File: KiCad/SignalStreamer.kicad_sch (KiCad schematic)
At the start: 24 parts, among them J101 Conn_01x01, J102 Conn_01x01, J103 Conn_01x01, J104 Conn_01x01, J105 Conn_01x02, T101 Coupled_Inductors_2

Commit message: Ver X1.0
Copied latest changes from backup project
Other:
- sheet Hardware: file untitled.kicad_sch -> hardware.kicad_sch
- title: 80m Vertical Dipole Fox Antenna -> 80m Bottom-Loaded Vertical Fox Antenna
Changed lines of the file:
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@@
 	(generator "eeschema")
 	(generator_version "9.0")
-	(paper "A4")
+	(paper "USLetter")
 	(title_block
-		(title "80m Vertical Dipole Fox Antenna")
-		(date "2025-12-30")
+		(title "80m Bottom-Loaded Vertical Fox Antenna")
+		(date "2026-01-02")
 		(rev "X1.0")
 	)
@@
 			)
 		)
+		(property "Sim.Enable" ""
+			(at 191.77 97.79 0)
+			(effects
+				(font
+					(size 1.27 1.27)
+				)
+				(hide yes)
+			)
+		)
 		(pin "1"
 		)
@@
 			)
 		)
+		(property "Sim.Enable" ""
+			(at 123.19 93.98 0)
+			(effects
+				(font
+					(size 1.27 1.27)
+				)
+				(hide yes)
+			)
+		)
 		(pin "4"
 		)
@@
 			)
 		)
+		(property "Sim.Enable" ""
+			(at 113.03 114.3 0)
+			(effects
+				(font
+					(size 1.27 1.27)
+				)
+				(hide yes)
+			)
+		)
 		(pin "1"
 		)
@@
 			)
 		)
-		(property "Sim.Device" ""
-			(at 218.44 97.79 0)
-			(effects
-				(font
-					(size 1.27 1.27)
-				)
-				(hide yes)
-			)
-		)
-		(property "Sim.Pins" ""
-			(at 218.44 97.79 0)
-			(effects
-				(font
-					(size 1.27 1.27)
-				)
-				(hide yes)
-			)
-		)
 		(property "Sim.Enable" ""
 			(at 218.44 97.79 0)
@@
 			)
 		)
+		(property "Sim.Enable" ""
+			(at 140.97 93.98 90)
+			(effects
+				(font
+					(size 1.27 1.27)
+				)
+				(hide yes)
+			)
+		)
 		(pin "1"
 		)
@@
 			)
 		)
-		(property "Sim.Device" ""
-			(at 241.3 97.79 0)
-			(effects
-				(font
-					(size 1.27 1.27)
-				)
-				(hide yes)
-			)
-		)
-		(property "Sim.Pins" ""
-			(at 241.3 97.79 0)
-			(effects
-				(font
-					(size 1.27 1.27)
-				)
-				(hide yes)
-			)
-		)
 		(property "Sim.Enable" ""
 			(at 241.3 97.79 0)
@@
 			)
 		)
-		(property "Sim.Device" ""
-			(at 229.87 97.79 0)
-			(effects
-				(font
-					(size 1.27 1.27)
-				)
-				(hide yes)
-			)
-		)
-		(property "Sim.Pins" ""
-			(at 229.87 97.79 0)
-			(effects
-				(font
-					(size 1.27 1.27)
-				)
-				(hide yes)
-			)
-		)
 		(property "Sim.Enable" ""
 			(at 229.87 97.79 0)
@@
 			)
 		)
-		(property "Sim.Device" ""
-			(at 205.74 97.79 0)
-			(effects
-				(font
-					(size 1.27 1.27)
-				)
-				(hide yes)
-			)
-		)
-		(property "Sim.Pins" ""
-			(at 205.74 97.79 0)
-			(effects
-				(font
-					(size 1.27 1.27)
-				)
-				(hide yes)
-			)
-		)
 		(property "Sim.Enable" ""
 			(at 205.74 97.79 0)
@@
 			)
 		)
+		(property "Sim.Enable" ""
+			(at 198.12 80.01 0)
+			(effects
+				(font
+					(size 1.27 1.27)
+				)
+				(hide yes)
+			)
+		)
 		(pin "2"
 		)
@@
 	)
 	(sheet
-		(at -19.05 6.35)
+		(at -25.4 5.08)
 		(size 16.51 11.43)
 		(exclude_from_sim yes)
@@
 		)
 		(property "Sheetname" "Hardware"
-			(at -19.05 5.6384 0)
+			(at -25.4 4.3684 0)
 			(effects
 				(font
@@
 			)
 		)
-		(property "Sheetfile" "untitled.kicad_sch"
-			(at -19.05 18.3646 0)
+		(property "Sheetfile" "hardware.kicad_sch"
+			(at -25.4 17.0946 0)
 			(effects
 				(font

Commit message: Development
Updates
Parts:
- L101: footprint Inductor_THT:L_Axial_L26.7mm_D14.0mm_P35.00mm_Horizontal_Vishay_IHA-104 -> Inductor_THT:L_Lipstick_Tube_Variable
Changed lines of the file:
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@@
-			)
-		)
-		(property "Sim.Enable" ""
-			(at 209.55 80.01 0)
-			(effects
-				(font
-					(size 1.27 1.27)
-				)
-				(hide yes)
 			)
 		)
@@
 			)
 		)
-		(property "Sim.Enable" ""
-			(at 191.77 97.79 0)
-			(effects
-				(font
-					(size 1.27 1.27)
-				)
-				(hide yes)
-			)
-		)
 		(pin "1"
 		)
@@
 		)
 		(property "Sim.Pins" ""
-			(at 123.19 153.67 90)
-			(effects
-				(font
-					(size 1.27 1.27)
-				)
-				(hide yes)
-			)
-		)
-		(property "Sim.Enable" ""
 			(at 123.19 153.67 90)
 			(effects
@@
 			)
 		)
-		(property "Sim.Enable" ""
-			(at 123.19 93.98 0)
-			(effects
-				(font
-					(size 1.27 1.27)
-				)
-				(hide yes)
-			)
-		)
 		(pin "4"
 		)
@@
 			)
 		)
-		(property "Footprint" "Inductor_THT:L_Axial_L26.7mm_D14.0mm_P35.00mm_Horizontal_Vishay_IHA-104"
+		(property "Footprint" "Inductor_THT:L_Lipstick_Tube_Variable"
 			(at 113.03 114.3 0)
 			(effects
@@
 		)
 		(property "Manufacturer PN" "FB-31-4852"
-			(at 113.03 114.3 0)
-			(effects
-				(font
-					(size 1.27 1.27)
-				)
-				(hide yes)
-			)
-		)
-		(property "Sim.Enable" ""
 			(at 113.03 114.3 0)
 			(effects
@@
 			)
 		)
-		(property "Sim.Enable" ""
-			(at 113.03 153.67 90)
-			(effects
-				(font
-					(size 1.27 1.27)
-				)
-				(hide yes)
-			)
-		)
 		(pin "1"
 		)
@@
 			)
 		)
-		(property "Sim.Enable" ""
-			(at 218.44 97.79 0)
-			(effects
-				(font
-					(size 1.27 1.27)
-				)
-				(hide yes)
-			)
-		)
 		(pin "1"
 		)
@@
 		(property "Link" "https://www.digikey.com/en/products/detail/tdk-corporation/FA14X7S2A474KRU06/5865817"
 			(at 154.94 93.98 90)
-			(effects
-				(font
-					(size 1.27 1.27)
-				)
-				(hide yes)
-			)
-		)
-		(property "Sim.Enable" ""
-			(at 154.94 93.98 0)
 			(effects
 				(font
@@
 			)
 		)
-		(property "Sim.Enable" ""
-			(at 140.97 93.98 90)
-			(effects
-				(font
-					(size 1.27 1.27)
-				)
-				(hide yes)
-			)
-		)
 		(pin "1"
 		)
@@
 		)
 		(property "Sim.Pins" ""
-			(at 163.83 129.54 0)
-			(effects
-				(font
-					(size 1.27 1.27)
-				)
-				(hide yes)
-			)
-		)
-		(property "Sim.Enable" ""
 			(at 163.83 129.54 0)
 			(effects
@@
 			)
 		)
-		(property "Sim.Enable" ""
-			(at 135.89 88.9 90)
-			(effects
-				(font
-					(size 1.27 1.27)
-				)
-				(hide yes)
-			)
-		)
 		(pin "2"
 		)
@@
 			)
 		)
-		(property "Sim.Enable" ""
-			(at 241.3 97.79 0)
-			(effects
-				(font
-					(size 1.27 1.27)
-				)
-				(hide yes)
-			)
-		)
 		(pin "1"
 		)
@@
 		)
 		(property "Manufacturer PN" "CF18JT470R"
-			(at 160.02 88.9 90)
-			(effects
-				(font
-					(size 1.27 1.27)
-				)
-				(hide yes)
-			)
-		)
-		(property "Sim.Enable" ""
 			(at 160.02 88.9 90)
 			(effects
@@
 			)
 		)
-		(property "Sim.Enable" ""
-			(at 107.95 83.82 0)
-			(effects
-				(font
-					(size 1.27 1.27)
-				)
-				(hide yes)
-			)
-		)
 		(pin "1"
 		)
@@
 			)
 		)
-		(property "Sim.Enable" ""
-			(at 113.03 40.64 0)
-			(effects
-				(font
-					(size 1.27 1.27)
-				)
-				(hide yes)
-			)
-		)
 		(pin "1"
 		)
@@
 			)
 		)
-		(property "Sim.Enable" ""
-			(at 229.87 97.79 0)
-			(effects
-				(font
-					(size 1.27 1.27)
-				)
-				(hide yes)
-			)
-		)
 		(pin "1"
 		)
@@
 			)
 		)
-		(property "Sim.Enable" ""
-			(at 198.12 88.9 0)
-			(effects
-				(font
-					(size 1.27 1.27)
-				)
-				(hide yes)
-			)
-		)
 		(pin "2"
 		)
@@
 			)
 		)
-		(property "Sim.Enable" ""
-			(at 205.74 97.79 0)
-			(effects
-				(font
-					(size 1.27 1.27)
-				)
-				(hide yes)
-			)
-		)
 		(pin "1"
 		)
@@
 			)
 		)
-		(property "Sim.Enable" ""
-			(at 236.22 80.01 0)
-			(effects
-				(font
-					(size 1.27 1.27)
-				)
-				(hide yes)
-			)
-		)
 		(pin "2"
 		)
@@
 			)
 		)
-		(property "Sim.Enable" ""
-			(at 148.59 88.9 0)
-			(effects
-				(font
-					(size 1.27 1.27)
-				)
-				(hide yes)
-			)
-		)
 		(pin "1"
 		)
@@
 			)
 		)
-		(property "Sim.Enable" ""
-			(at 224.79 80.01 0)
-			(effects
-				(font
-					(size 1.27 1.27)
-				)
-				(hide yes)
-			)
-		)
 		(pin "2"
 		)
@@
 			)
 		)
-		(property "Sim.Enable" ""
-			(at 198.12 80.01 0)
-			(effects
-				(font
-					(size 1.27 1.27)
-				)
-				(hide yes)
-			)
-		)
 		(pin "2"
 		)
@@
 			)
 		)
-		(property "Sim.Enable" ""
-			(at 118.11 153.67 90)
-			(effects
-				(font
-					(size 1.27 1.27)
-				)
-				(hide yes)
-			)
-		)
 		(pin "1"
 		)
@@
 			(at 170.18 88.9 90)
 			(effects
-				(font
-					(size 1.27 1.27)
-				)
-				(hide yes)
-			)
-		)
-		(property "Sim.Enable" ""
-			(at 170.18 88.9 90)
-			(effects

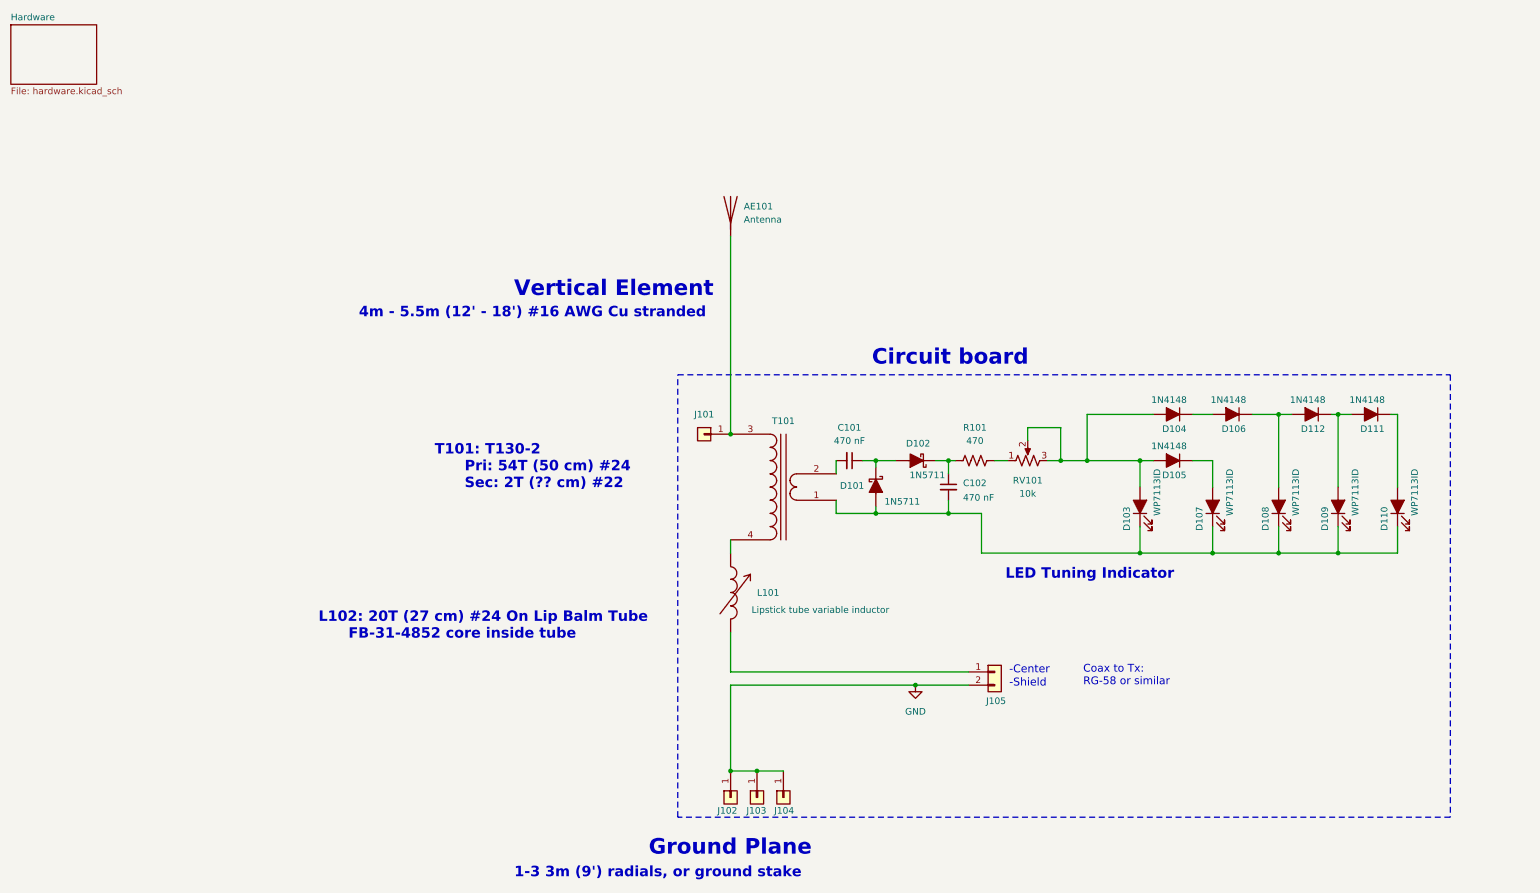
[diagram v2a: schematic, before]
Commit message: Ver 1.0
Redesign of LED tuning indicator. All gerbers updated.
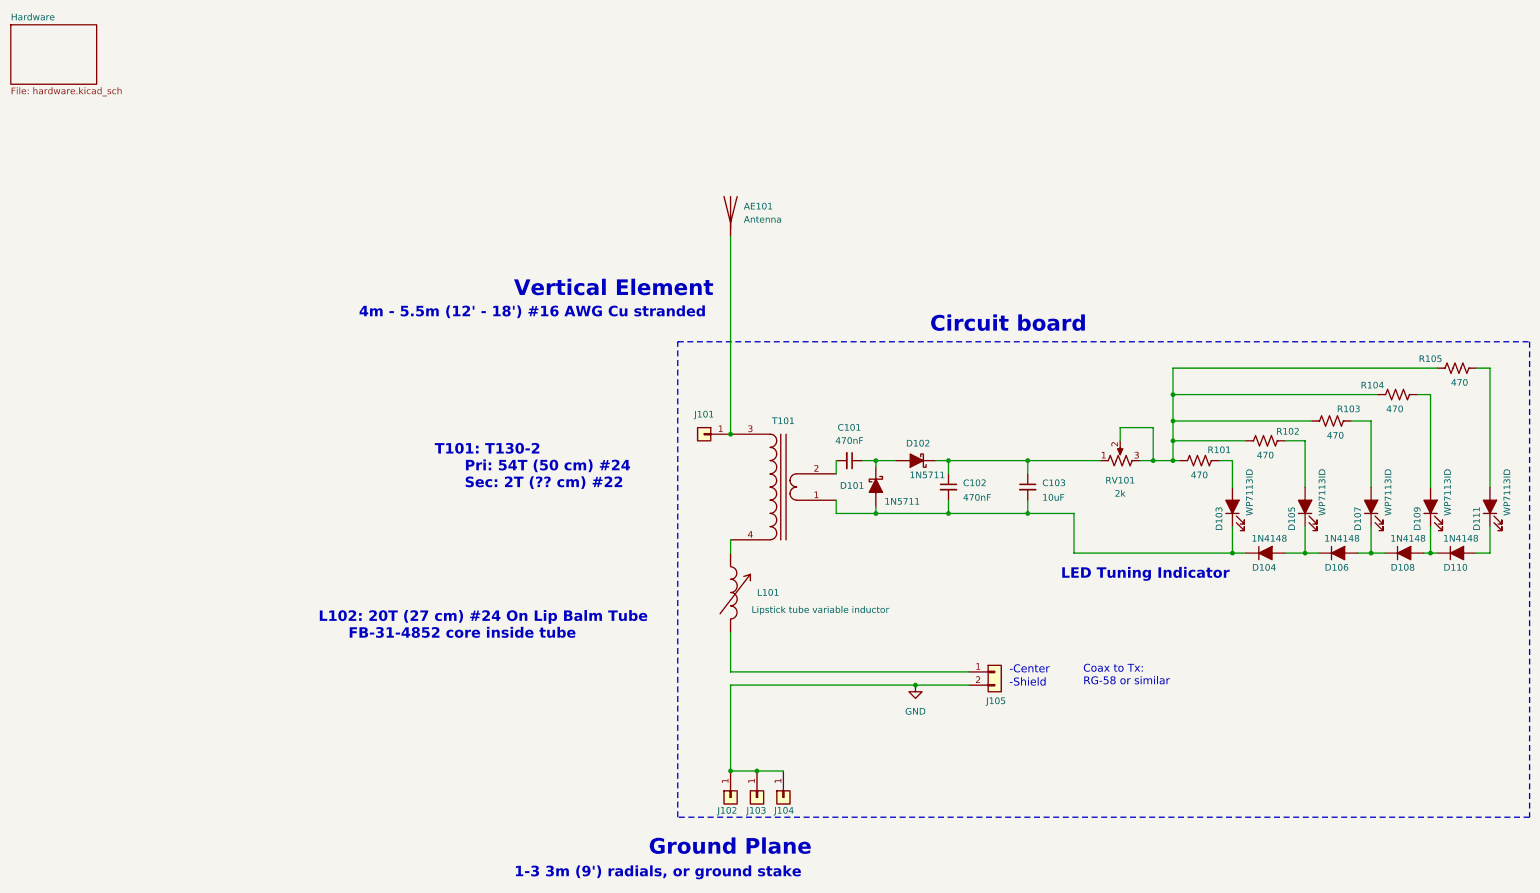
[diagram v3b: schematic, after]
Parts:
- removed D105: 1N4148, Diode_THT:D_DO-35_SOD27_P2.54mm_Vertical_KathodeUp, symbol Diode:1N4148WT
- added C103: 10uF, Capacitor_THT:CP_Radial_Tantal_D5.5mm_P2.50mm, symbol Device:C_Small
- added R102, R103, R104, R105: 470, Resistor_THT:R_Axial_DIN0207_L6.3mm_D2.5mm_P5.08mm_Vertical, symbol Device:R_US
- C101, C102: value 470 nF -> 470nF
- R101: footprint Resistor_THT:R_Axial_DIN0207_L6.3mm_D2.5mm_P7.62mm_Horizontal -> Resistor_THT:R_Axial_DIN0207_L6.3mm_D2.5mm_P5.08mm_Vertical
- RV101: value 10k -> 2k; Digi-Key Part No. 3296W-103LF-ND -> 118-PV36W202C01B00-ND; Link https://www.digikey.com/en/products/detail/bourns-inc/3296W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 -> https://www.digikey.com/en/products/detail/bourns-inc/PV36W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; Manufacturer PN 3296W-1-103LF -> PV36W202C01B00
- renumbered D107 to D105, D108 to D107, D112 to D108, D111 to D110, D110 to D111
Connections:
- net at D106.2 (A): now also D107.1 (K), D108.1 (K); no longer D104.1 (K)
- net at C102.2, D101.2 (A), D103.1 (K)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: now also D104.1 (K), C103.2; no longer D105.1 (K), D107.1 (K), D109.1 (K), D111.1 (K)
- net at RV101.2, RV101.3: now also R101.1, R102.1, R103.1, R104.1, R105.1; no longer D103.2 (A), D104.2 (A)
- net at C102.1, D102.1 (K): now also RV101.1, C103.1; no longer R101.1
- net at D111.2 (A): now also R105.2; no longer D110.1 (K)
- net at R101.2: now also D103.2 (A); no longer RV101.1
- net at D105.2 (A): now also R102.2
- new net: D104.2 (A), D105.1 (K), D106.1 (K)
- new net: D107.2 (A), R103.2
- new net: D109.2 (A), R104.2
- new net: D110.2 (A), D111.1 (K)
- new net: D108.2 (A), D109.1 (K), D110.1 (K)
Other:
- moved on the sheet: D103, D104, D105, D106, D107, D108, D109, D110, D111, R101, RV101
